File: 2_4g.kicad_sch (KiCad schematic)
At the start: 6 parts, among them J2 BWSMA-KWE-Z001

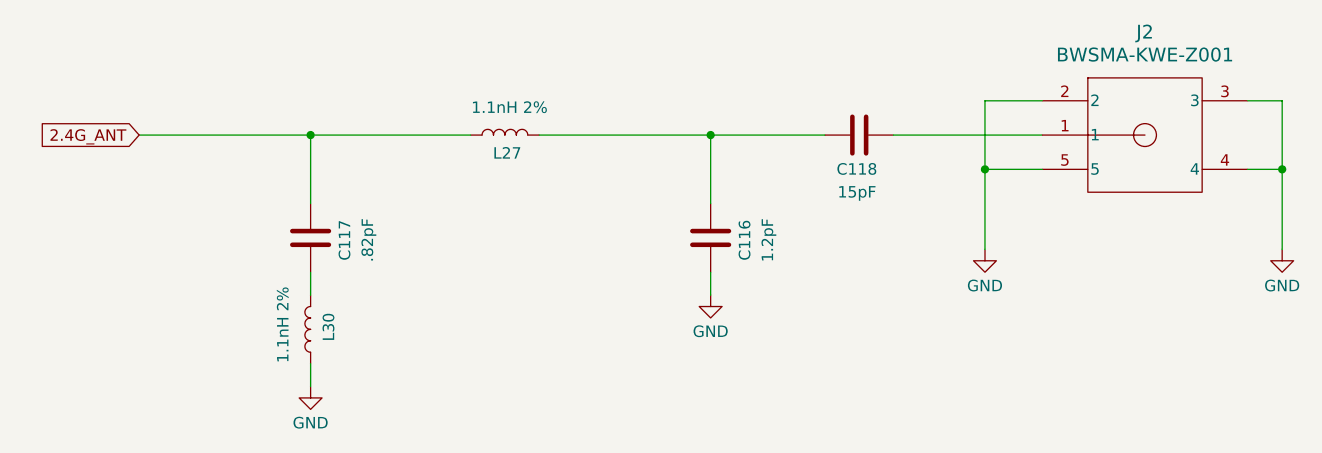
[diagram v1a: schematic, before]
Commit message: Fix a wrong component value on 2.5GHz
Signed-off-by: Corey Minyard <corey@minyard.net>
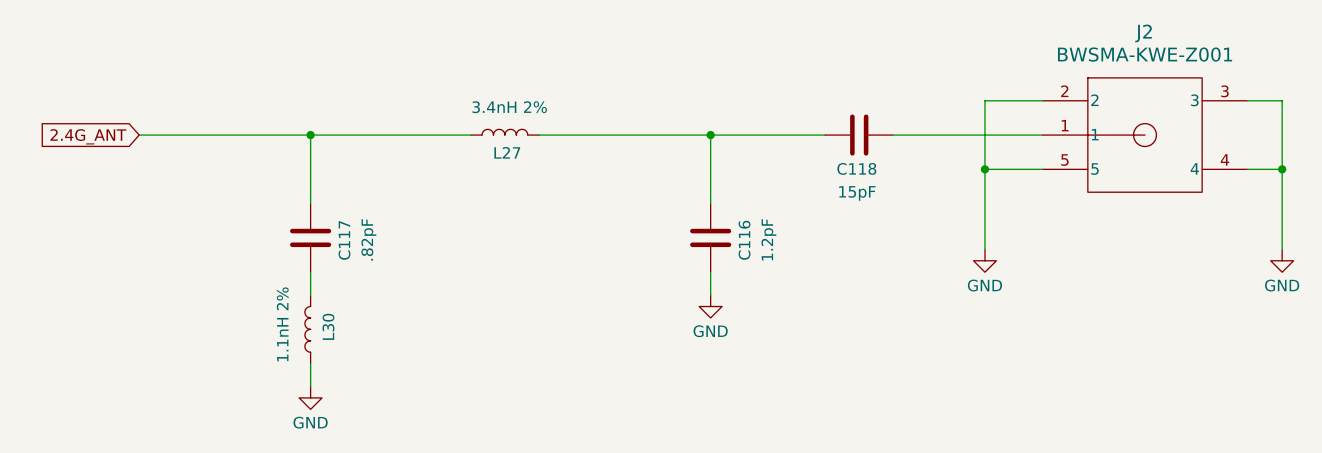
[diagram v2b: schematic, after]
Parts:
- L27: value 1.1nH 2% -> 3.4nH 2%; footprint Inductor_SMD:L_0805_2012Metric_Pad1.05x1.20mm_HandSolder -> Inductor_SMD:L_0402_1005Metric_Pad0.77x0.64mm_HandSolder
- L30: footprint Inductor_SMD:L_0805_2012Metric_Pad1.05x1.20mm_HandSolder -> Inductor_SMD:L_0402_1005Metric_Pad0.77x0.64mm_HandSolder
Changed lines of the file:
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@@
 			)
 		)
-		(property "Footprint" "Inductor_SMD:L_0805_2012Metric_Pad1.05x1.20mm_HandSolder"
+		(property "Footprint" "Inductor_SMD:L_0402_1005Metric_Pad0.77x0.64mm_HandSolder"
 			(at 78.74 120.65 0)
 			(effects
@@
 			)
 		)
-		(property "Value" "1.1nH 2%"
+		(property "Value" "3.4nH 2%"
 			(at 100.838 96.012 90)
 			(effects
@@
 			)
 		)
-		(property "Footprint" "Inductor_SMD:L_0805_2012Metric_Pad1.05x1.20mm_HandSolder"
+		(property "Footprint" "Inductor_SMD:L_0402_1005Metric_Pad0.77x0.64mm_HandSolder"
 			(at 100.33 99.06 0)
 			(effects
